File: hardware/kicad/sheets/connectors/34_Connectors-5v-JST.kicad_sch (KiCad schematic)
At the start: 10 parts, among them Q71 L2N7002SLLT1G, Q72 AO3401A, U216 TPS22965DSGR

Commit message: reorganized
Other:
- title: Connectors-5v-JST -> 5V JST Outputs
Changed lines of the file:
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@@
 	(paper "User" 297 210)
 	(title_block
-		(title "Connectors-5v-JST")
+		(title "5V JST Outputs")
 		(date "2026-02-16")
 	)
@@
 		(on_board yes)
 		(dnp no)
-		(property "Reference" "U216"
+		(property "Reference" "U?"
 			(at 149.86 64.77 0)
 			(effects
@@
 				(path "/3f85abf4-0b95-4c4a-b7e9-06f59ca1ea3d/0597c19e-4e57-4183-a7ff-6a300a521a92/9ed2a1cc-b4f2-4f0d-8c3f-2b2e0f2f5034"
 					(reference "U216")
+					(unit 1)
+				)
+			)
+			(project "1_Connectors"
+				(path "/907d2c43-ff0f-4be5-b1b7-1b4093ecff75/9ed2a1cc-b4f2-4f0d-8c3f-2b2e0f2f5034"
+					(reference "U?")
 					(unit 1)
 				)
@@
 		(on_board yes)
 		(dnp no)
-		(property "Reference" "#PWR0315"
+		(property "Reference" "#PWR?"
 			(at 133.35 64.77 0)
 			(effects
@@
 				(path "/3f85abf4-0b95-4c4a-b7e9-06f59ca1ea3d/0597c19e-4e57-4183-a7ff-6a300a521a92/9ed2a1cc-b4f2-4f0d-8c3f-2b2e0f2f5034"
 					(reference "#PWR0315")
+					(unit 1)
+				)
+			)
+			(project "1_Connectors"
+				(path "/907d2c43-ff0f-4be5-b1b7-1b4093ecff75/9ed2a1cc-b4f2-4f0d-8c3f-2b2e0f2f5034"
+					(reference "#PWR?")
 					(unit 1)
 				)
@@
 		(on_board yes)
 		(dnp no)
-		(property "Reference" "R563"
+		(property "Reference" "R?"
 			(at 115.57 82.55 90)
 			(effects
@@
 				(path "/3f85abf4-0b95-4c4a-b7e9-06f59ca1ea3d/0597c19e-4e57-4183-a7ff-6a300a521a92/9ed2a1cc-b4f2-4f0d-8c3f-2b2e0f2f5034"
 					(reference "R563")
+					(unit 1)
+				)
+			)
+			(project "1_Connectors"
+				(path "/907d2c43-ff0f-4be5-b1b7-1b4093ecff75/9ed2a1cc-b4f2-4f0d-8c3f-2b2e0f2f5034"
+					(reference "R?")
 					(unit 1)
 				)
@@
 		(on_board yes)
 		(dnp no)
-		(property "Reference" "R559"
+		(property "Reference" "R?"
 			(at 125.73 137.16 90)
 			(effects
@@
 				(path "/3f85abf4-0b95-4c4a-b7e9-06f59ca1ea3d/0597c19e-4e57-4183-a7ff-6a300a521a92/9ed2a1cc-b4f2-4f0d-8c3f-2b2e0f2f5034"
 					(reference "R559")
+					(unit 1)
+				)
+			)
+			(project "1_Connectors"
+				(path "/907d2c43-ff0f-4be5-b1b7-1b4093ecff75/9ed2a1cc-b4f2-4f0d-8c3f-2b2e0f2f5034"
+					(reference "R?")
 					(unit 1)
 				)
@@
 		(on_board yes)
 		(dnp no)
-		(property "Reference" "#PWR0317"
+		(property "Reference" "#PWR?"
 			(at 120.65 92.71 0)
 			(effects
@@
 				(path "/3f85abf4-0b95-4c4a-b7e9-06f59ca1ea3d/0597c19e-4e57-4183-a7ff-6a300a521a92/9ed2a1cc-b4f2-4f0d-8c3f-2b2e0f2f5034"
 					(reference "#PWR0317")
+					(unit 1)
+				)
+			)
+			(project "1_Connectors"
+				(path "/907d2c43-ff0f-4be5-b1b7-1b4093ecff75/9ed2a1cc-b4f2-4f0d-8c3f-2b2e0f2f5034"
+					(reference "#PWR?")
 					(unit 1)
 				)
@@
 		(on_board yes)
 		(dnp no)
-		(property "Reference" "R560"
+		(property "Reference" "R?"
 			(at 142.24 111.76 0)
 			(effects
@@
 				(path "/3f85abf4-0b95-4c4a-b7e9-06f59ca1ea3d/0597c19e-4e57-4183-a7ff-6a300a521a92/9ed2a1cc-b4f2-4f0d-8c3f-2b2e0f2f5034"
 					(reference "R560")
+					(unit 1)
+				)
+			)
+			(project "1_Connectors"
+				(path "/907d2c43-ff0f-4be5-b1b7-1b4093ecff75/9ed2a1cc-b4f2-4f0d-8c3f-2b2e0f2f5034"
+					(reference "R?")
 					(unit 1)
 				)
@@
 		(on_board yes)
 		(dnp no)
-		(property "Reference" "R561"
+		(property "Reference" "R?"
 			(at 111.76 127 0)
 			(effects
@@
 				(path "/3f85abf4-0b95-4c4a-b7e9-06f59ca1ea3d/0597c19e-4e57-4183-a7ff-6a300a521a92/9ed2a1cc-b4f2-4f0d-8c3f-2b2e0f2f5034"
 					(reference "R561")
+					(unit 1)
+				)
+			)
+			(project "1_Connectors"
+				(path "/907d2c43-ff0f-4be5-b1b7-1b4093ecff75/9ed2a1cc-b4f2-4f0d-8c3f-2b2e0f2f5034"
+					(reference "R?")
 					(unit 1)
 				)
@@
 		(on_board yes)
 		(dnp no)
-		(property "Reference" "D88"
+		(property "Reference" "D?"
 			(at 130.81 83.82 90)
 			(effects
@@
 				(path "/3f85abf4-0b95-4c4a-b7e9-06f59ca1ea3d/0597c19e-4e57-4183-a7ff-6a300a521a92/9ed2a1cc-b4f2-4f0d-8c3f-2b2e0f2f5034"
 					(reference "D88")
+					(unit 1)
+				)
+			)
+			(project "1_Connectors"
+				(path "/907d2c43-ff0f-4be5-b1b7-1b4093ecff75/9ed2a1cc-b4f2-4f0d-8c3f-2b2e0f2f5034"
+					(reference "D?")
 					(unit 1)
 				)
@@
 		(on_board yes)
 		(dnp no)
-		(property "Reference" "Q72"
+		(property "Reference" "Q?"
 			(at 151.13 99.06 90)
 			(effects
@@
 				(path "/3f85abf4-0b95-4c4a-b7e9-06f59ca1ea3d/0597c19e-4e57-4183-a7ff-6a300a521a92/9ed2a1cc-b4f2-4f0d-8c3f-2b2e0f2f5034"
 					(reference "Q72")
+					(unit 1)
+				)
+			)
+			(project "1_Connectors"
+				(path "/907d2c43-ff0f-4be5-b1b7-1b4093ecff75/9ed2a1cc-b4f2-4f0d-8c3f-2b2e0f2f5034"
+					(reference "Q?")
 					(unit 1)
 				)
@@
 		(on_board yes)
 		(dnp no)
-		(property "Reference" "#PWR0313"
+		(property "Reference" "#PWR?"
 			(at 146.05 146.05 0)
 			(effects
@@
 				(path "/3f85abf4-0b95-4c4a-b7e9-06f59ca1ea3d/0597c19e-4e57-4183-a7ff-6a300a521a92/9ed2a1cc-b4f2-4f0d-8c3f-2b2e0f2f5034"
 					(reference "#PWR0313")
+					(unit 1)
+				)
+			)
+			(project "1_Connectors"
+				(path "/907d2c43-ff0f-4be5-b1b7-1b4093ecff75/9ed2a1cc-b4f2-4f0d-8c3f-2b2e0f2f5034"
+					(reference "#PWR?")
 					(unit 1)
 				)
@@
 		(on_board yes)
 		(dnp no)
-		(property "Reference" "R562"
+		(property "Reference" "R?"
 			(at 115.57 67.31 90)
 			(effects
@@
 				(path "/3f85abf4-0b95-4c4a-b7e9-06f59ca1ea3d/0597c19e-4e57-4183-a7ff-6a300a521a92/9ed2a1cc-b4f2-4f0d-8c3f-2b2e0f2f5034"
 					(reference "R562")
+					(unit 1)
+				)
+			)
+			(project "1_Connectors"
+				(path "/907d2c43-ff0f-4be5-b1b7-1b4093ecff75/9ed2a1cc-b4f2-4f0d-8c3f-2b2e0f2f5034"
+					(reference "R?")
 					(unit 1)
 				)
@@
 		(on_board yes)
 		(dnp no)
-		(property "Reference" "D87"
+		(property "Reference" "D?"
 			(at 139.7 137.16 90)
 			(effects
@@
 				(path "/3f85abf4-0b95-4c4a-b7e9-06f59ca1ea3d/0597c19e-4e57-4183-a7ff-6a300a521a92/9ed2a1cc-b4f2-4f0d-8c3f-2b2e0f2f5034"
 					(reference "D87")
+					(unit 1)
+				)
+			)
+			(project "1_Connectors"
+				(path "/907d2c43-ff0f-4be5-b1b7-1b4093ecff75/9ed2a1cc-b4f2-4f0d-8c3f-2b2e0f2f5034"
+					(reference "D?")
 					(unit 1)
 				)
@@
 		(on_board yes)
 		(dnp no)
-		(property "Reference" "#PWR0314"
+		(property "Reference" "#PWR?"
 			(at 104.14 124.46 0)
 			(effects
@@
 				(path "/3f85abf4-0b95-4c4a-b7e9-06f59ca1ea3d/0597c19e-4e57-4183-a7ff-6a300a521a92/9ed2a1cc-b4f2-4f0d-8c3f-2b2e0f2f5034"
 					(reference "#PWR0314")
+					(unit 1)
+				)
+			)
+			(project "1_Connectors"
+				(path "/907d2c43-ff0f-4be5-b1b7-1b4093ecff75/9ed2a1cc-b4f2-4f0d-8c3f-2b2e0f2f5034"
+					(reference "#PWR?")
 					(unit 1)
 				)
@@
 		(on_board yes)
 		(dnp no)
-		(property "Reference" "Q71"
+		(property "Reference" "Q?"
 			(at 158.75 123.19 0)
 			(effects
@@
 				(path "/3f85abf4-0b95-4c4a-b7e9-06f59ca1ea3d/0597c19e-4e57-4183-a7ff-6a300a521a92/9ed2a1cc-b4f2-4f0d-8c3f-2b2e0f2f5034"
 					(reference "Q71")
+					(unit 1)
+				)
+			)
+			(project "1_Connectors"
+				(path "/907d2c43-ff0f-4be5-b1b7-1b4093ecff75/9ed2a1cc-b4f2-4f0d-8c3f-2b2e0f2f5034"
+					(reference "Q?")
 					(unit 1)
 				)
@@
 		(on_board yes)
 		(dnp no)
-		(property "Reference" "#PWR0316"
+		(property "Reference" "#PWR?"
 			(at 113.03 62.23 0)
 			(effects
@@
 					(unit 1)
 				)
+			)
+			(project "1_Connectors"
+				(path "/907d2c43-ff0f-4be5-b1b7-1b4093ecff75/9ed2a1cc-b4f2-4f0d-8c3f-2b2e0f2f5034"
+					(reference "#PWR?")
+					(unit 1)
+				)

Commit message: before final cleanup
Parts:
- renumbered D88 to D36, D87 to D37, Q72 to Q17, Q71 to Q18, R562 to R176, R563 to R177, R561 to R178, R559 to R179, R560 to R180, U216 to U53
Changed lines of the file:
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@@
 		(on_board yes)
 		(dnp no)
-		(property "Reference" "U?"
+		(property "Reference" "U53"
 			(at 149.86 64.77 0)
 			(effects
@@
 		)
 		(instances
-			(project ""
-				(path "/3f85abf4-0b95-4c4a-b7e9-06f59ca1ea3d/0597c19e-4e57-4183-a7ff-6a300a521a92/9ed2a1cc-b4f2-4f0d-8c3f-2b2e0f2f5034"
-					(reference "U216")
+			(project "svea_powerboard_rev3"
+				(path "/3f85abf4-0b95-4c4a-b7e9-06f59ca1ea3d/5c2e021f-c2d4-49e2-8c36-9a64f1f12005/8d05c3b8-20a4-4a7f-9b20-01f8d5d5be51/9ed2a1cc-b4f2-4f0d-8c3f-2b2e0f2f5034"
+					(reference "U53")
 					(unit 1)
 				)
@@
 		(on_board yes)
 		(dnp no)
-		(property "Reference" "#PWR?"
+		(property "Reference" "#PWR0264"
 			(at 133.35 64.77 0)
 			(effects
@@
 		)
 		(instances
-			(project ""
-				(path "/3f85abf4-0b95-4c4a-b7e9-06f59ca1ea3d/0597c19e-4e57-4183-a7ff-6a300a521a92/9ed2a1cc-b4f2-4f0d-8c3f-2b2e0f2f5034"
-					(reference "#PWR0315")
+			(project "svea_powerboard_rev3"
+				(path "/3f85abf4-0b95-4c4a-b7e9-06f59ca1ea3d/5c2e021f-c2d4-49e2-8c36-9a64f1f12005/8d05c3b8-20a4-4a7f-9b20-01f8d5d5be51/9ed2a1cc-b4f2-4f0d-8c3f-2b2e0f2f5034"
+					(reference "#PWR0264")
 					(unit 1)
 				)
@@
 		(on_board yes)
 		(dnp no)
-		(property "Reference" "R?"
+		(property "Reference" "R177"
 			(at 115.57 82.55 90)
 			(effects
@@
 		)
 		(instances
-			(project ""
-				(path "/3f85abf4-0b95-4c4a-b7e9-06f59ca1ea3d/0597c19e-4e57-4183-a7ff-6a300a521a92/9ed2a1cc-b4f2-4f0d-8c3f-2b2e0f2f5034"
-					(reference "R563")
+			(project "svea_powerboard_rev3"
+				(path "/3f85abf4-0b95-4c4a-b7e9-06f59ca1ea3d/5c2e021f-c2d4-49e2-8c36-9a64f1f12005/8d05c3b8-20a4-4a7f-9b20-01f8d5d5be51/9ed2a1cc-b4f2-4f0d-8c3f-2b2e0f2f5034"
+					(reference "R177")
 					(unit 1)
 				)
@@
 		(on_board yes)
 		(dnp no)
-		(property "Reference" "R?"
+		(property "Reference" "R179"
 			(at 125.73 137.16 90)
 			(effects
@@
 		)
 		(instances
-			(project ""
-				(path "/3f85abf4-0b95-4c4a-b7e9-06f59ca1ea3d/0597c19e-4e57-4183-a7ff-6a300a521a92/9ed2a1cc-b4f2-4f0d-8c3f-2b2e0f2f5034"
-					(reference "R559")
+			(project "svea_powerboard_rev3"
+				(path "/3f85abf4-0b95-4c4a-b7e9-06f59ca1ea3d/5c2e021f-c2d4-49e2-8c36-9a64f1f12005/8d05c3b8-20a4-4a7f-9b20-01f8d5d5be51/9ed2a1cc-b4f2-4f0d-8c3f-2b2e0f2f5034"
+					(reference "R179")
 					(unit 1)
 				)
@@
 		(on_board yes)
 		(dnp no)
-		(property "Reference" "#PWR?"
+		(property "Reference" "#PWR0263"
 			(at 120.65 92.71 0)
 			(effects
@@
 		)
 		(instances
-			(project ""
-				(path "/3f85abf4-0b95-4c4a-b7e9-06f59ca1ea3d/0597c19e-4e57-4183-a7ff-6a300a521a92/9ed2a1cc-b4f2-4f0d-8c3f-2b2e0f2f5034"
-					(reference "#PWR0317")
+			(project "svea_powerboard_rev3"
+				(path "/3f85abf4-0b95-4c4a-b7e9-06f59ca1ea3d/5c2e021f-c2d4-49e2-8c36-9a64f1f12005/8d05c3b8-20a4-4a7f-9b20-01f8d5d5be51/9ed2a1cc-b4f2-4f0d-8c3f-2b2e0f2f5034"
+					(reference "#PWR0263")
 					(unit 1)
 				)
@@
 		(on_board yes)
 		(dnp no)
-		(property "Reference" "R?"
+		(property "Reference" "R180"
 			(at 142.24 111.76 0)
 			(effects
@@
 		)
 		(instances
-			(project ""
-				(path "/3f85abf4-0b95-4c4a-b7e9-06f59ca1ea3d/0597c19e-4e57-4183-a7ff-6a300a521a92/9ed2a1cc-b4f2-4f0d-8c3f-2b2e0f2f5034"
-					(reference "R560")
+			(project "svea_powerboard_rev3"
+				(path "/3f85abf4-0b95-4c4a-b7e9-06f59ca1ea3d/5c2e021f-c2d4-49e2-8c36-9a64f1f12005/8d05c3b8-20a4-4a7f-9b20-01f8d5d5be51/9ed2a1cc-b4f2-4f0d-8c3f-2b2e0f2f5034"
+					(reference "R180")
 					(unit 1)
 				)
@@
 		(on_board yes)
 		(dnp no)
-		(property "Reference" "R?"
+		(property "Reference" "R178"
 			(at 111.76 127 0)
 			(effects
@@
 		)
 		(instances
-			(project ""
-				(path "/3f85abf4-0b95-4c4a-b7e9-06f59ca1ea3d/0597c19e-4e57-4183-a7ff-6a300a521a92/9ed2a1cc-b4f2-4f0d-8c3f-2b2e0f2f5034"
-					(reference "R561")
+			(project "svea_powerboard_rev3"
+				(path "/3f85abf4-0b95-4c4a-b7e9-06f59ca1ea3d/5c2e021f-c2d4-49e2-8c36-9a64f1f12005/8d05c3b8-20a4-4a7f-9b20-01f8d5d5be51/9ed2a1cc-b4f2-4f0d-8c3f-2b2e0f2f5034"
+					(reference "R178")
 					(unit 1)
 				)
@@
 		(on_board yes)
 		(dnp no)
-		(property "Reference" "D?"
+		(property "Reference" "D36"
 			(at 130.81 83.82 90)
 			(effects
@@
 		)
 		(instances
-			(project ""
-				(path "/3f85abf4-0b95-4c4a-b7e9-06f59ca1ea3d/0597c19e-4e57-4183-a7ff-6a300a521a92/9ed2a1cc-b4f2-4f0d-8c3f-2b2e0f2f5034"
-					(reference "D88")
+			(project "svea_powerboard_rev3"
+				(path "/3f85abf4-0b95-4c4a-b7e9-06f59ca1ea3d/5c2e021f-c2d4-49e2-8c36-9a64f1f12005/8d05c3b8-20a4-4a7f-9b20-01f8d5d5be51/9ed2a1cc-b4f2-4f0d-8c3f-2b2e0f2f5034"
+					(reference "D36")
 					(unit 1)
 				)
@@
 		(on_board yes)
 		(dnp no)
-		(property "Reference" "Q?"
+		(property "Reference" "Q17"
 			(at 151.13 99.06 90)
 			(effects
@@
 		)
 		(instances
-			(project ""
-				(path "/3f85abf4-0b95-4c4a-b7e9-06f59ca1ea3d/0597c19e-4e57-4183-a7ff-6a300a521a92/9ed2a1cc-b4f2-4f0d-8c3f-2b2e0f2f5034"
-					(reference "Q72")
+			(project "svea_powerboard_rev3"
+				(path "/3f85abf4-0b95-4c4a-b7e9-06f59ca1ea3d/5c2e021f-c2d4-49e2-8c36-9a64f1f12005/8d05c3b8-20a4-4a7f-9b20-01f8d5d5be51/9ed2a1cc-b4f2-4f0d-8c3f-2b2e0f2f5034"
+					(reference "Q17")
 					(unit 1)
 				)
@@
 		(on_board yes)
 		(dnp no)
-		(property "Reference" "#PWR?"
+		(property "Reference" "#PWR0262"
 			(at 146.05 146.05 0)
 			(effects
@@
 		)
 		(instances
-			(project ""
-				(path "/3f85abf4-0b95-4c4a-b7e9-06f59ca1ea3d/0597c19e-4e57-4183-a7ff-6a300a521a92/9ed2a1cc-b4f2-4f0d-8c3f-2b2e0f2f5034"
-					(reference "#PWR0313")
+			(project "svea_powerboard_rev3"
+				(path "/3f85abf4-0b95-4c4a-b7e9-06f59ca1ea3d/5c2e021f-c2d4-49e2-8c36-9a64f1f12005/8d05c3b8-20a4-4a7f-9b20-01f8d5d5be51/9ed2a1cc-b4f2-4f0d-8c3f-2b2e0f2f5034"
+					(reference "#PWR0262")
 					(unit 1)
 				)
@@
 		(on_board yes)
 		(dnp no)
-		(property "Reference" "R?"
+		(property "Reference" "R176"
 			(at 115.57 67.31 90)
 			(effects
@@
 		)
 		(instances
-			(project ""
-				(path "/3f85abf4-0b95-4c4a-b7e9-06f59ca1ea3d/0597c19e-4e57-4183-a7ff-6a300a521a92/9ed2a1cc-b4f2-4f0d-8c3f-2b2e0f2f5034"
-					(reference "R562")
+			(project "svea_powerboard_rev3"
+				(path "/3f85abf4-0b95-4c4a-b7e9-06f59ca1ea3d/5c2e021f-c2d4-49e2-8c36-9a64f1f12005/8d05c3b8-20a4-4a7f-9b20-01f8d5d5be51/9ed2a1cc-b4f2-4f0d-8c3f-2b2e0f2f5034"
+					(reference "R176")
 					(unit 1)
 				)
@@
 		(on_board yes)
 		(dnp no)
-		(property "Reference" "D?"
+		(property "Reference" "D37"
 			(at 139.7 137.16 90)
 			(effects
@@
 		)
 		(instances
-			(project ""
-				(path "/3f85abf4-0b95-4c4a-b7e9-06f59ca1ea3d/0597c19e-4e57-4183-a7ff-6a300a521a92/9ed2a1cc-b4f2-4f0d-8c3f-2b2e0f2f5034"
-					(reference "D87")
+			(project "svea_powerboard_rev3"
+				(path "/3f85abf4-0b95-4c4a-b7e9-06f59ca1ea3d/5c2e021f-c2d4-49e2-8c36-9a64f1f12005/8d05c3b8-20a4-4a7f-9b20-01f8d5d5be51/9ed2a1cc-b4f2-4f0d-8c3f-2b2e0f2f5034"
+					(reference "D37")
 					(unit 1)
 				)
@@
 		(on_board yes)
 		(dnp no)
-		(property "Reference" "#PWR?"
+		(property "Reference" "#PWR0261"
 			(at 104.14 124.46 0)
 			(effects
@@
 		)
 		(instances
-			(project ""
-				(path "/3f85abf4-0b95-4c4a-b7e9-06f59ca1ea3d/0597c19e-4e57-4183-a7ff-6a300a521a92/9ed2a1cc-b4f2-4f0d-8c3f-2b2e0f2f5034"
-					(reference "#PWR0314")
+			(project "svea_powerboard_rev3"
+				(path "/3f85abf4-0b95-4c4a-b7e9-06f59ca1ea3d/5c2e021f-c2d4-49e2-8c36-9a64f1f12005/8d05c3b8-20a4-4a7f-9b20-01f8d5d5be51/9ed2a1cc-b4f2-4f0d-8c3f-2b2e0f2f5034"
+					(reference "#PWR0261")
 					(unit 1)
 				)
@@
 		(on_board yes)
 		(dnp no)
-		(property "Reference" "Q?"
+		(property "Reference" "Q18"
 			(at 158.75 123.19 0)
 			(effects
@@
 		)
 		(instances
-			(project ""
-				(path "/3f85abf4-0b95-4c4a-b7e9-06f59ca1ea3d/0597c19e-4e57-4183-a7ff-6a300a521a92/9ed2a1cc-b4f2-4f0d-8c3f-2b2e0f2f5034"
-					(reference "Q71")
+			(project "svea_powerboard_rev3"
+				(path "/3f85abf4-0b95-4c4a-b7e9-06f59ca1ea3d/5c2e021f-c2d4-49e2-8c36-9a64f1f12005/8d05c3b8-20a4-4a7f-9b20-01f8d5d5be51/9ed2a1cc-b4f2-4f0d-8c3f-2b2e0f2f5034"
+					(reference "Q18")
 					(unit 1)
 				)
@@
 		(on_board yes)
 		(dnp no)
-		(property "Reference" "#PWR?"
+		(property "Reference" "#PWR0265"
 			(at 113.03 62.23 0)
 			(effects
@@
 		)
 		(instances
-			(project ""
-				(path "/3f85abf4-0b95-4c4a-b7e9-06f59ca1ea3d/0597c19e-4e57-4183-a7ff-6a300a521a92/9ed2a1cc-b4f2-4f0d-8c3f-2b2e0f2f5034"
-					(reference "#PWR0316")
-					(unit 1)
-				)
+			(project "svea_powerboard_rev3"
+				(path "/3f85abf4-0b95-4c4a-b7e9-06f59ca1ea3d/5c2e021f-c2d4-49e2-8c36-9a64f1f12005/8d05c3b8-20a4-4a7f-9b20-01f8d5d5be51/9ed2a1cc-b4f2-4f0d-8c3f-2b2e0f2f5034"
+					(reference "#PWR0265")
+					(unit 1)
+				)

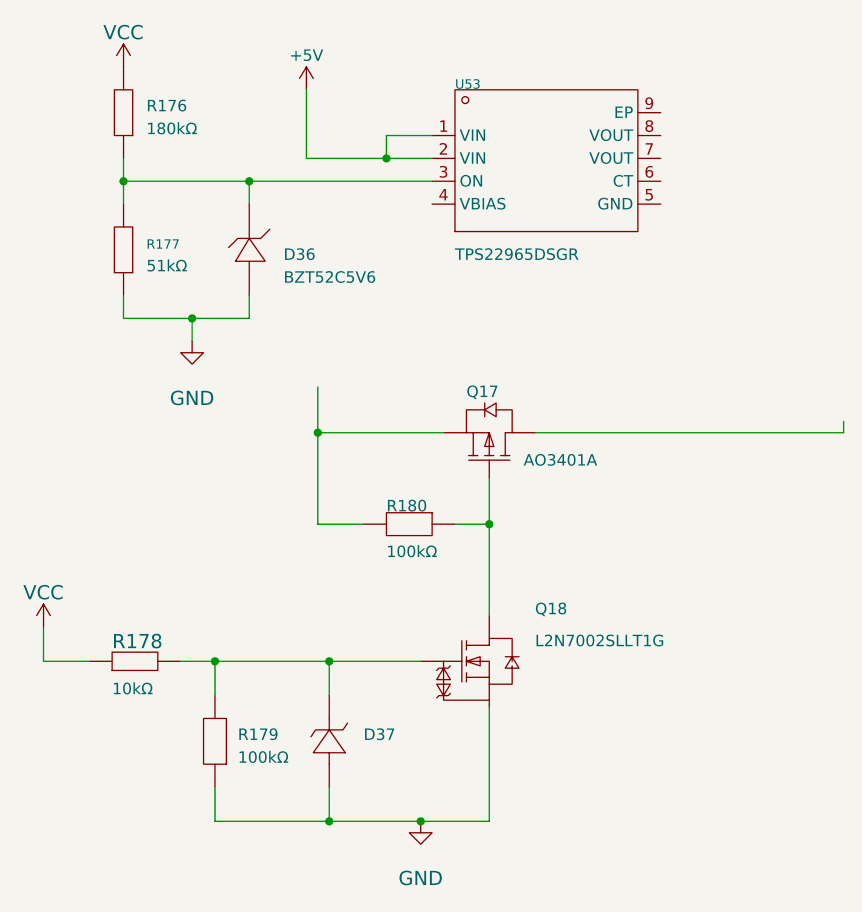
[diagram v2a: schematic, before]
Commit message: better sheet nesting for power rails
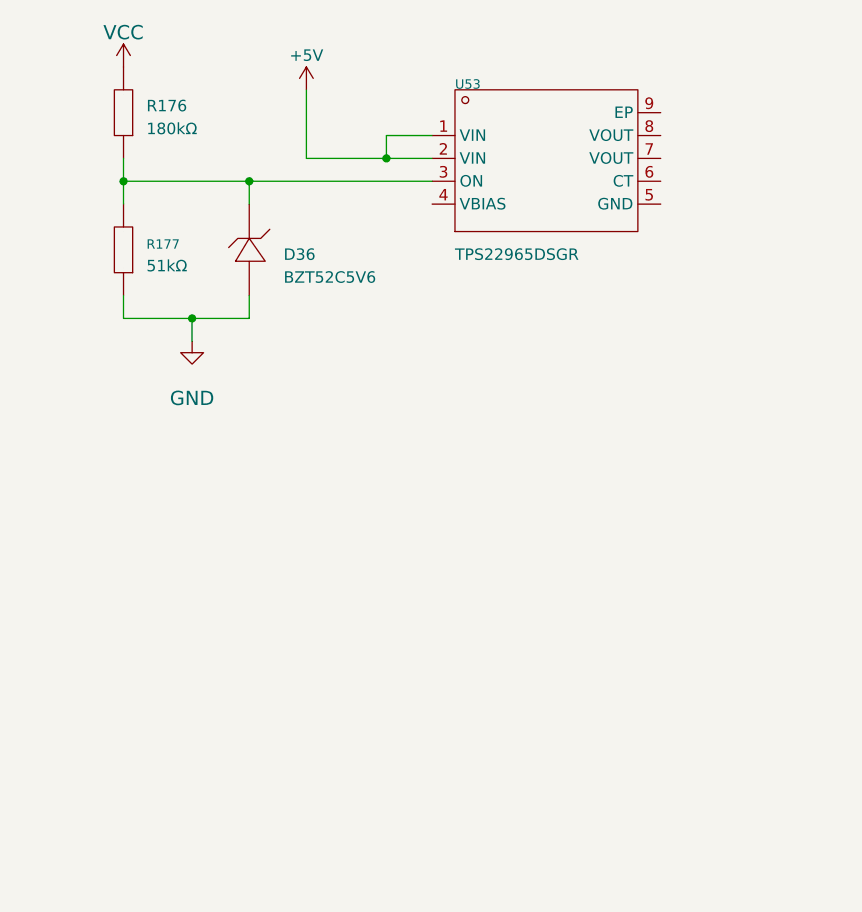
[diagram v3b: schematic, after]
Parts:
- removed D37: MMSZ5242B, Diode_SMD:SOD-123, symbol 5v rail sm-easyedapro:MMSZ5242B_C19077426
- removed Q17: AO3401A, Package_TO_SOT_SMD:SOT-23, symbol 5v rail sm-easyedapro:AO3401A_C347476
- removed Q18: L2N7002SLLT1G, Package_TO_SOT_SMD:SOT-23, symbol 5v rail sm-easyedapro:L2N7002SLLT1G
- removed R178: 10kΩ, Resistor_SMD:R_0603_1608Metric, symbol 5v rail sm-easyedapro:0603WAF1002T5E
- removed R179, R180: 100kΩ, Resistor_SMD:R_0603_1608Metric, symbol 5v rail sm-easyedapro:FRC0603J104 TS
